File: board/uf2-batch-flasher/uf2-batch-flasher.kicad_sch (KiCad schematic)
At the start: 7 parts, among them SW101 SW_MEC_5E, U102 FSUSB74, U103 74HC238, U104 RaspberryPi_Pico_W

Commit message: Briefly document and add the OSHW logo.
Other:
- company: (none) -> nbp.name
- title: (none) -> UF2 Batch Flasher
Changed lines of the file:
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@@
 (kicad_sch (version 20230121) (generator eeschema)
   (paper "A4")
+  (title_block
+    (title "UF2 Batch Flasher")
+    (date "2023-10-20")
+    (rev "0.1")
+    (company "nbp.name")
+    (comment 2 "selecting and flashing each device.")
+    (comment 3 "This page contains the first layer with the Raspberry Pi Pico W in charge of")
+    (comment 4 "UF2 Batch Flasher is a USB hub for flashing USB devices")
+  )
   (junction (at 38.1 151.13) (diameter 0) (color 0 0 0 0)
   )

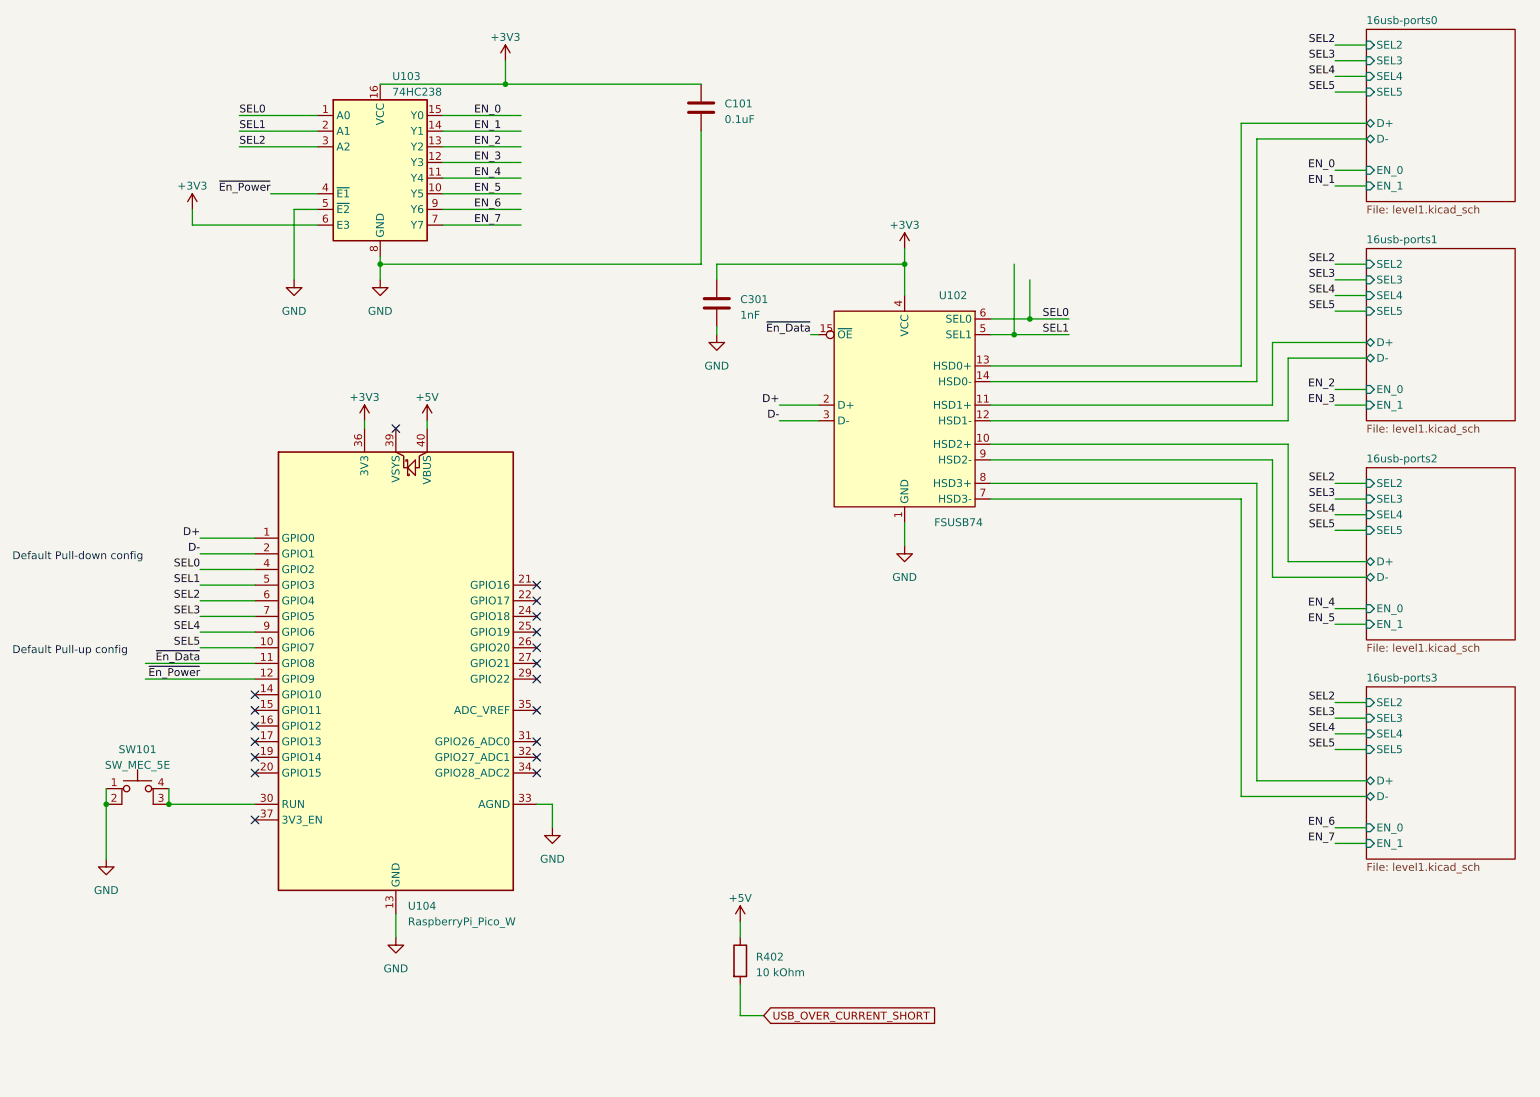
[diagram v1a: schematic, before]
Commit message: Fix Select pins mapping.
Both the selector and demultiplexer are used to enable/disable the power
and data pins. If the mapping of pins is not identical between the 2
then we would enable the power pins of one USB port and the data pins of
another.

This patch changes that such that components which are closer to the
Pico are using the high-power bits while components which are further
down the tree are using the low bits. This way the enable pins are
correctly ordered as specified in the datasheets of both components.

Previously we were using the lowest bits, this would have been if
the enable pins were mapped accordingly. Which was not the case.

This change include changes in the schematics and in the board layout.
The component remain at their original placement.

This change also adds the OSHW logo as well as the fiducial in the
schematic such that they are not removed each time we re-import the
schematics in the board.
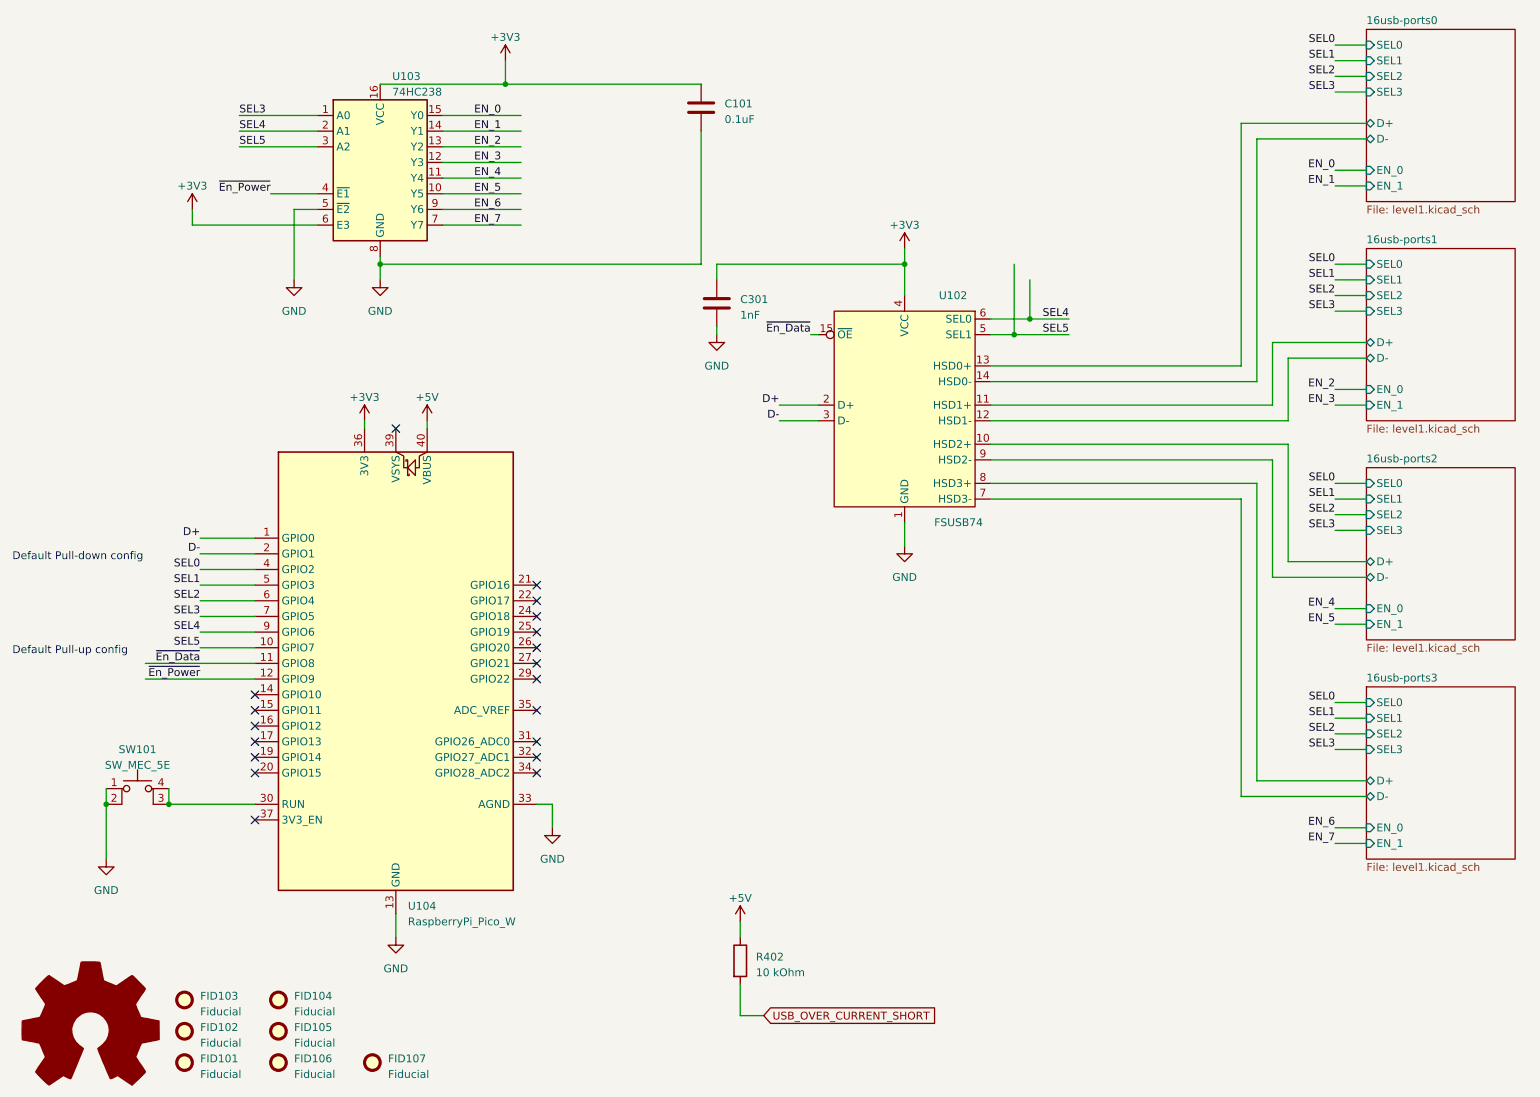
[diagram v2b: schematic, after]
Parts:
- added FID101, FID102, FID103, FID104, FID105, FID106, FID107: Fiducial, Fiducial:Fiducial_1mm_Mask2mm, symbol Mechanical:Fiducial
- added SYM101: Logo_Open_Hardware_Large, Symbol:OSHW-Logo_11.4x12mm_SilkScreen, symbol Graphic:Logo_Open_Hardware_Large
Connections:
- net SEL0: no longer U102.6 (SEL0), U103.1 (A0)
- net SEL1: no longer U102.5 (SEL1), U103.2 (A1)
- net SEL2: no longer U103.3 (A2)
- net SEL3: now also U103.1 (A0)
- net SEL4: now also U102.6 (SEL0), U103.2 (A1)
- net SEL5: now also U102.5 (SEL1), U103.3 (A2)
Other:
- sheet 16usb-ports0 ports: added SEL0, SEL1; removed SEL4, SEL5
- sheet 16usb-ports1 ports: added SEL0, SEL1; removed SEL4, SEL5
- sheet 16usb-ports2 ports: added SEL0, SEL1; removed SEL4, SEL5
- sheet 16usb-ports3 ports: added SEL0, SEL1; removed SEL4, SEL5
